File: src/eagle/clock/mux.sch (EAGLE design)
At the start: 51 parts, among them U1 SN74HC595N, U2 SN74HC595N, U3 SN74HC595N

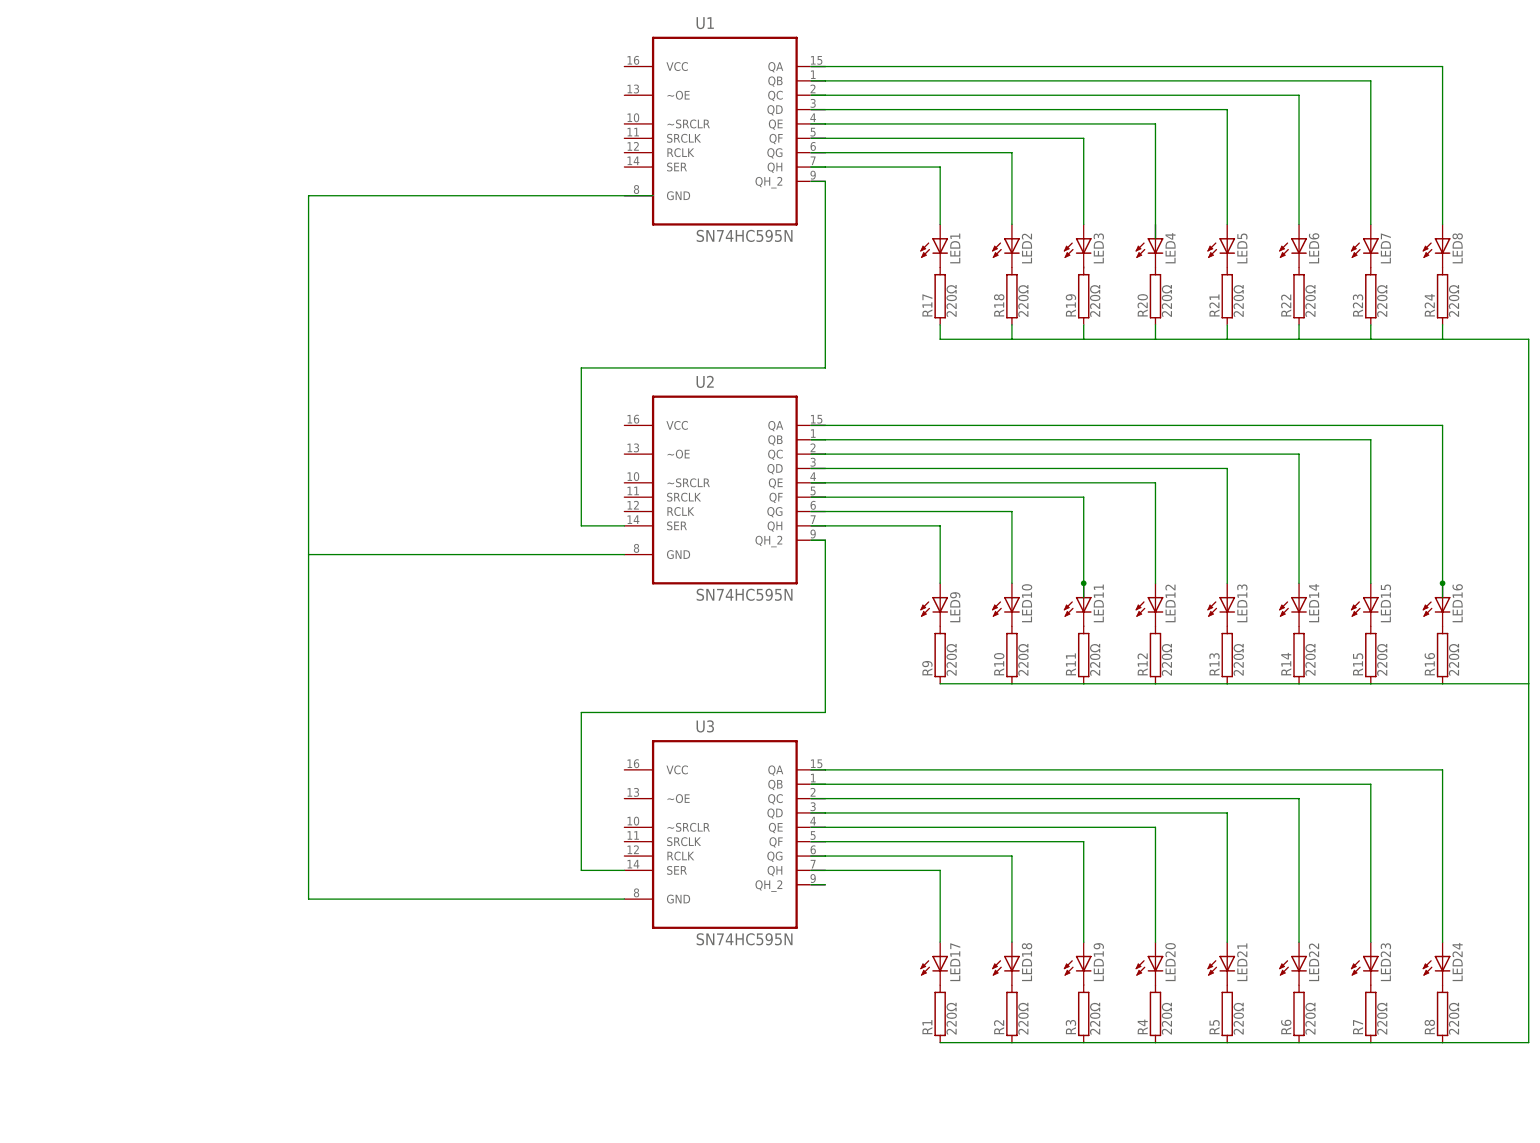
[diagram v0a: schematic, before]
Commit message: Add junctions to LEDs, SRs, and resistors
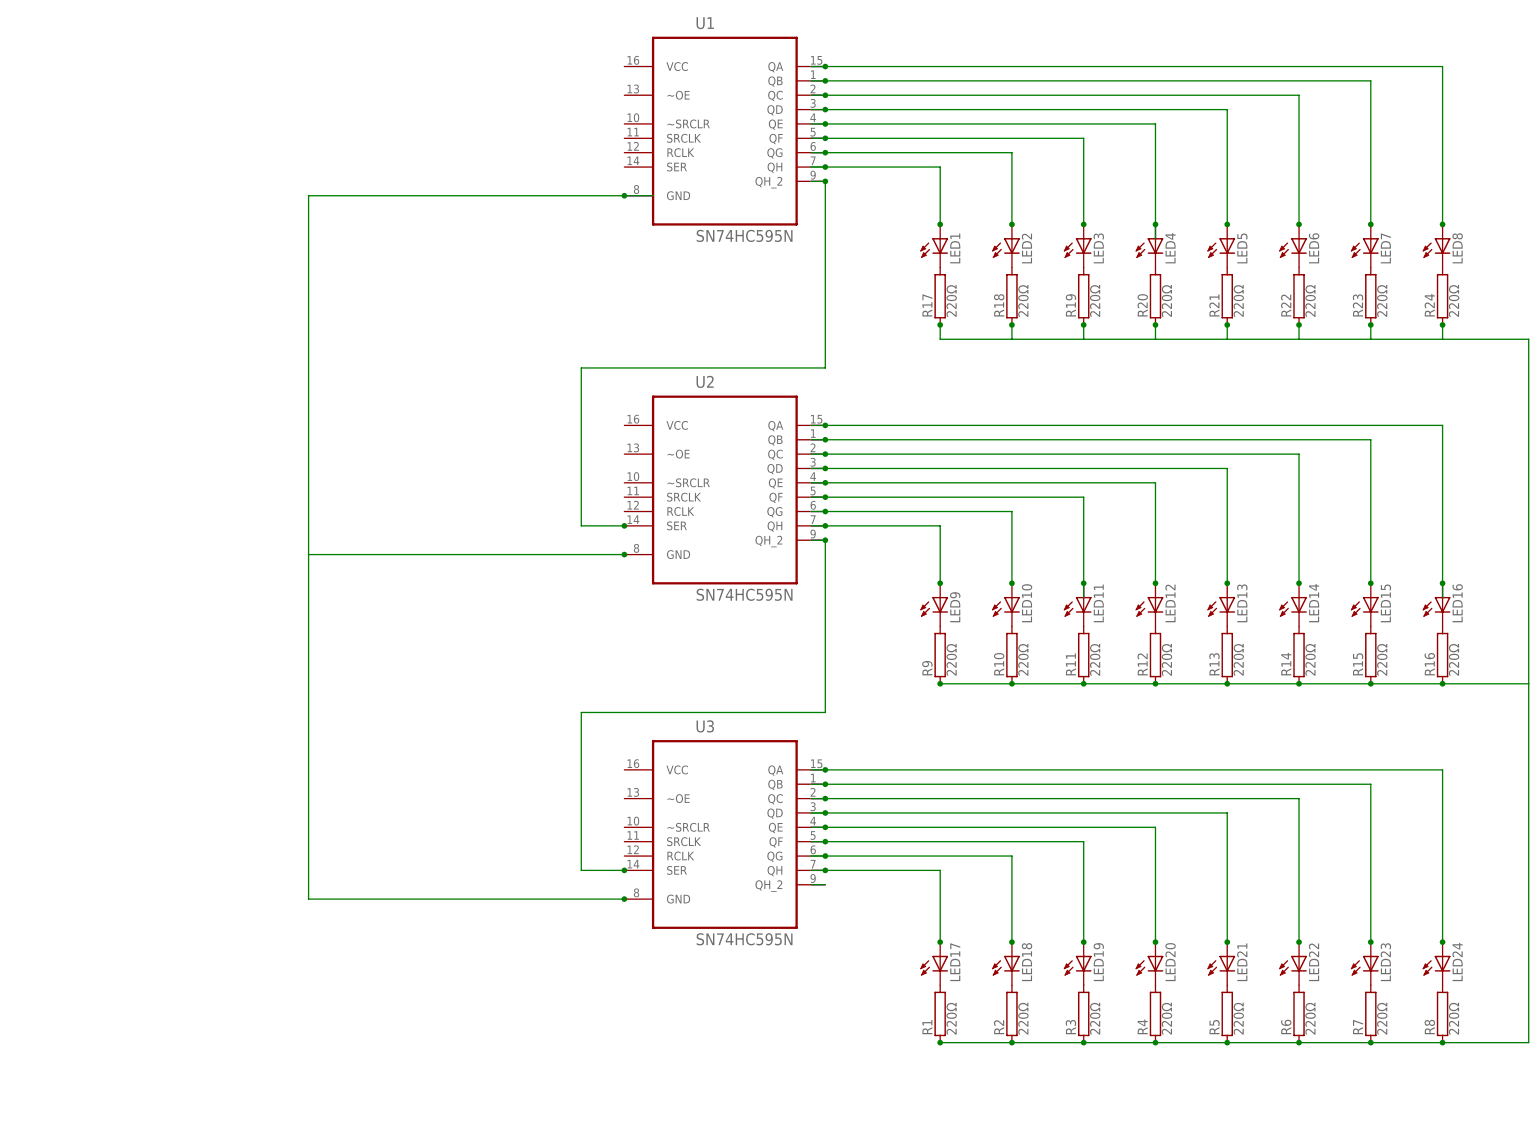
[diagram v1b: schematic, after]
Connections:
- net N$25: now also U1.QH_2
- net N$46: now also U1.GND
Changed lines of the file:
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@@
 <wire x1="152.4" y1="12.7" x2="165.1" y2="12.7" width="0.1524" layer="91"/>
 <wire x1="165.1" y1="15.24" x2="165.1" y2="12.7" width="0.1524" layer="91"/>
+<junction x="76.2" y="-48.26"/>
+<junction x="88.9" y="-48.26"/>
+<junction x="101.6" y="-48.26"/>
+<junction x="114.3" y="-48.26"/>
+<junction x="127" y="-48.26"/>
+<junction x="139.7" y="-48.26"/>
+<junction x="152.4" y="-48.26"/>
+<junction x="165.1" y="-48.26"/>
+<junction x="165.1" y="15.24"/>
+<junction x="152.4" y="15.24"/>
+<junction x="139.7" y="15.24"/>
+<junction x="127" y="15.24"/>
+<junction x="114.3" y="15.24"/>
+<junction x="101.6" y="15.24"/>
+<junction x="88.9" y="15.24"/>
+<junction x="76.2" y="15.24"/>
+<junction x="76.2" y="-111.76"/>
+<junction x="88.9" y="-111.76"/>
+<junction x="101.6" y="-111.76"/>
+<junction x="114.3" y="-111.76"/>
+<junction x="127" y="-111.76"/>
+<junction x="139.7" y="-111.76"/>
+<junction x="152.4" y="-111.76"/>
+<junction x="165.1" y="-111.76"/>
 </segment>
 </net>
@@
 <wire x1="55.88" y1="60.96" x2="165.1" y2="60.96" width="0.1524" layer="91"/>
 <wire x1="165.1" y1="60.96" x2="165.1" y2="33.02" width="0.1524" layer="91"/>
+<junction x="55.88" y="60.96"/>
+<junction x="165.1" y="33.02"/>
 </segment>
 </net>
@@
 <wire x1="55.88" y1="43.18" x2="76.2" y2="43.18" width="0.1524" layer="91"/>
 <wire x1="76.2" y1="43.18" x2="76.2" y2="33.02" width="0.1524" layer="91"/>
+<junction x="55.88" y="43.18"/>
+<junction x="76.2" y="33.02"/>
 </segment>
 </net>
@@
 <wire x1="55.88" y1="45.72" x2="88.9" y2="45.72" width="0.1524" layer="91"/>
 <wire x1="88.9" y1="45.72" x2="88.9" y2="33.02" width="0.1524" layer="91"/>
+<junction x="55.88" y="45.72"/>
+<junction x="88.9" y="33.02"/>
 </segment>
 </net>
@@
 <wire x1="55.88" y1="48.26" x2="101.6" y2="48.26" width="0.1524" layer="91"/>
 <wire x1="101.6" y1="48.26" x2="101.6" y2="33.02" width="0.1524" layer="91"/>
+<junction x="55.88" y="48.26"/>
+<junction x="101.6" y="33.02"/>
 </segment>
 </net>
@@
 <wire x1="55.88" y1="50.8" x2="114.3" y2="50.8" width="0.1524" layer="91"/>
 <wire x1="114.3" y1="50.8" x2="114.3" y2="33.02" width="0.1524" layer="91"/>
+<junction x="55.88" y="50.8"/>
+<junction x="114.3" y="33.02"/>
 </segment>
 </net>
@@
 <wire x1="55.88" y1="53.34" x2="127" y2="53.34" width="0.1524" layer="91"/>
 <wire x1="127" y1="53.34" x2="127" y2="33.02" width="0.1524" layer="91"/>
+<junction x="55.88" y="53.34"/>
+<junction x="127" y="33.02"/>
 </segment>
 </net>
@@
 <wire x1="55.88" y1="58.42" x2="152.4" y2="58.42" width="0.1524" layer="91"/>
 <wire x1="152.4" y1="58.42" x2="152.4" y2="33.02" width="0.1524" layer="91"/>
+<junction x="55.88" y="58.42"/>
+<junction x="152.4" y="33.02"/>
 </segment>
 </net>
@@
 <wire x1="55.88" y1="55.88" x2="139.7" y2="55.88" width="0.1524" layer="91"/>
 <wire x1="139.7" y1="55.88" x2="139.7" y2="33.02" width="0.1524" layer="91"/>
+<junction x="55.88" y="55.88"/>
+<junction x="139.7" y="33.02"/>
 </segment>
 </net>
@@
 <wire x1="55.88" y1="-7.62" x2="139.7" y2="-7.62" width="0.1524" layer="91"/>
 <wire x1="139.7" y1="-7.62" x2="139.7" y2="-30.48" width="0.1524" layer="91"/>
+<junction x="55.88" y="-7.62"/>
+<junction x="139.7" y="-30.48"/>
 </segment>
 </net>
@@
 <wire x1="55.88" y1="-5.08" x2="152.4" y2="-5.08" width="0.1524" layer="91"/>
 <wire x1="152.4" y1="-5.08" x2="152.4" y2="-30.48" width="0.1524" layer="91"/>
+<junction x="55.88" y="-5.08"/>
+<junction x="152.4" y="-30.48"/>
 </segment>
 </net>
@@
 <wire x1="165.1" y1="-30.48" x2="165.1" y2="-33.02" width="0.1524" layer="91"/>
 <junction x="165.1" y="-30.48"/>
+<junction x="55.88" y="-2.54"/>
 </segment>
 </net>
@@
 <wire x1="55.88" y1="-10.16" x2="127" y2="-10.16" width="0.1524" layer="91"/>
 <wire x1="127" y1="-10.16" x2="127" y2="-30.48" width="0.1524" layer="91"/>
+<junction x="55.88" y="-10.16"/>
+<junction x="127" y="-30.48"/>
 </segment>
 </net>
@@
 <wire x1="55.88" y1="-12.7" x2="114.3" y2="-12.7" width="0.1524" layer="91"/>
 <wire x1="114.3" y1="-12.7" x2="114.3" y2="-30.48" width="0.1524" layer="91"/>
+<junction x="55.88" y="-12.7"/>
+<junction x="114.3" y="-30.48"/>
 </segment>
 </net>
@@
 <wire x1="55.88" y1="-17.78" x2="88.9" y2="-17.78" width="0.1524" layer="91"/>
 <wire x1="88.9" y1="-17.78" x2="88.9" y2="-30.48" width="0.1524" layer="91"/>
+<junction x="55.88" y="-17.78"/>
+<junction x="88.9" y="-30.48"/>
 </segment>
 </net>
@@
 <wire x1="55.88" y1="-20.32" x2="76.2" y2="-20.32" width="0.1524" layer="91"/>
 <wire x1="76.2" y1="-20.32" x2="76.2" y2="-30.48" width="0.1524" layer="91"/>
+<junction x="55.88" y="-20.32"/>
+<junction x="76.2" y="-30.48"/>
 </segment>
 </net>
@@
 <wire x1="101.6" y1="-30.48" x2="101.6" y2="-33.02" width="0.1524" layer="91"/>
 <junction x="101.6" y="-30.48"/>
+<junction x="55.88" y="-15.24"/>
 </segment>
 </net>
@@
 <wire x1="55.88" y1="-78.74" x2="88.9" y2="-78.74" width="0.1524" layer="91"/>
 <wire x1="88.9" y1="-78.74" x2="88.9" y2="-93.98" width="0.1524" layer="91"/>
+<junction x="55.88" y="-78.74"/>
+<junction x="88.9" y="-93.98"/>
 </segment>
 </net>
@@
 <wire x1="55.88" y1="-76.2" x2="101.6" y2="-76.2" width="0.1524" layer="91"/>
 <wire x1="101.6" y1="-76.2" x2="101.6" y2="-93.98" width="0.1524" layer="91"/>
+<junction x="55.88" y="-76.2"/>
+<junction x="101.6" y="-93.98"/>
 </segment>
 </net>
@@
 <wire x1="55.88" y1="-71.12" x2="127" y2="-71.12" width="0.1524" layer="91"/>
 <wire x1="127" y1="-71.12" x2="127" y2="-93.98" width="0.1524" layer="91"/>
+<junction x="55.88" y="-71.12"/>
+<junction x="127" y="-93.98"/>
 </segment>
 </net>
@@
 <wire x1="55.88" y1="-68.58" x2="139.7" y2="-68.58" width="0.1524" layer="91"/>
 <wire x1="139.7" y1="-68.58" x2="139.7" y2="-93.98" width="0.1524" layer="91"/>
+<junction x="55.88" y="-68.58"/>
+<junction x="139.7" y="-93.98"/>
 </segment>
 </net>
@@
 <wire x1="55.88" y1="-66.04" x2="152.4" y2="-66.04" width="0.1524" layer="91"/>
 <wire x1="152.4" y1="-66.04" x2="152.4" y2="-93.98" width="0.1524" layer="91"/>
+<junction x="55.88" y="-66.04"/>
+<junction x="152.4" y="-93.98"/>
 </segment>
 </net>
@@
 <wire x1="55.88" y1="-63.5" x2="165.1" y2="-63.5" width="0.1524" layer="91"/>
 <wire x1="165.1" y1="-63.5" x2="165.1" y2="-93.98" width="0.1524" layer="91"/>
+<junction x="55.88" y="-63.5"/>
+<junction x="165.1" y="-93.98"/>
 </segment>
 </net>
@@
 <wire x1="55.88" y1="-73.66" x2="114.3" y2="-73.66" width="0.1524" layer="91"/>
 <wire x1="114.3" y1="-73.66" x2="114.3" y2="-93.98" width="0.1524" layer="91"/>
+<junction x="55.88" y="-73.66"/>
+<junction x="114.3" y="-93.98"/>
 </segment>
 </net>
@@
 <wire x1="55.88" y1="-81.28" x2="76.2" y2="-81.28" width="0.1524" layer="91"/>
 <wire x1="76.2" y1="-81.28" x2="76.2" y2="-93.98" width="0.1524" layer="91"/>
+<junction x="55.88" y="-81.28"/>
+<junction x="76.2" y="-93.98"/>
 </segment>
 </net>
@@
 <pinref part="U2" gate="A" pin="SER"/>
 <wire x1="12.7" y1="-20.32" x2="20.32" y2="-20.32" width="0.1524" layer="91"/>
+<pinref part="U1" gate="A" pin="QH_2"/>
+<junction x="55.88" y="40.64"/>
+<junction x="20.32" y="-20.32"/>
 </segment>
 </net>
@@
 <pinref part="U3" gate="A" pin="SER"/>
 <wire x1="12.7" y1="-81.28" x2="20.32" y2="-81.28" width="0.1524" layer="91"/>
+<junction x="55.88" y="-22.86"/>
+<junction x="20.32" y="-81.28"/>
 </segment>
 </net>
@@
 <net name="N$46" class="0">
 <segment>
-<wire x1="25.4" y1="38.1" x2="-35.56" y2="38.1" width="0.1524" layer="91"/>
+<wire x1="25.4" y1="38.1" x2="20.32" y2="38.1" width="0.1524" layer="91"/>
+<wire x1="20.32" y1="38.1" x2="-35.56" y2="38.1" width="0.1524" layer="91"/>
 <wire x1="-35.56" y1="38.1" x2="-35.56" y2="-25.4" width="0.1524" layer="91"/>
 <pinref part="U2" gate="A" pin="GND"/>
@@
 <pinref part="U3" gate="A" pin="GND"/>
 <wire x1="-35.56" y1="-86.36" x2="20.32" y2="-86.36" width="0.1524" layer="91"/>
-</segment>
-</net>
+<pinref part="U1" gate="A" pin="GND"/>
+<junction x="20.32" y="38.1"/>
+<junction x="20.32" y="-25.4"/>
+<junction x="20.32" y="-86.36"/>
+</segment>
+</net>

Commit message: Add Arduino in/out mock
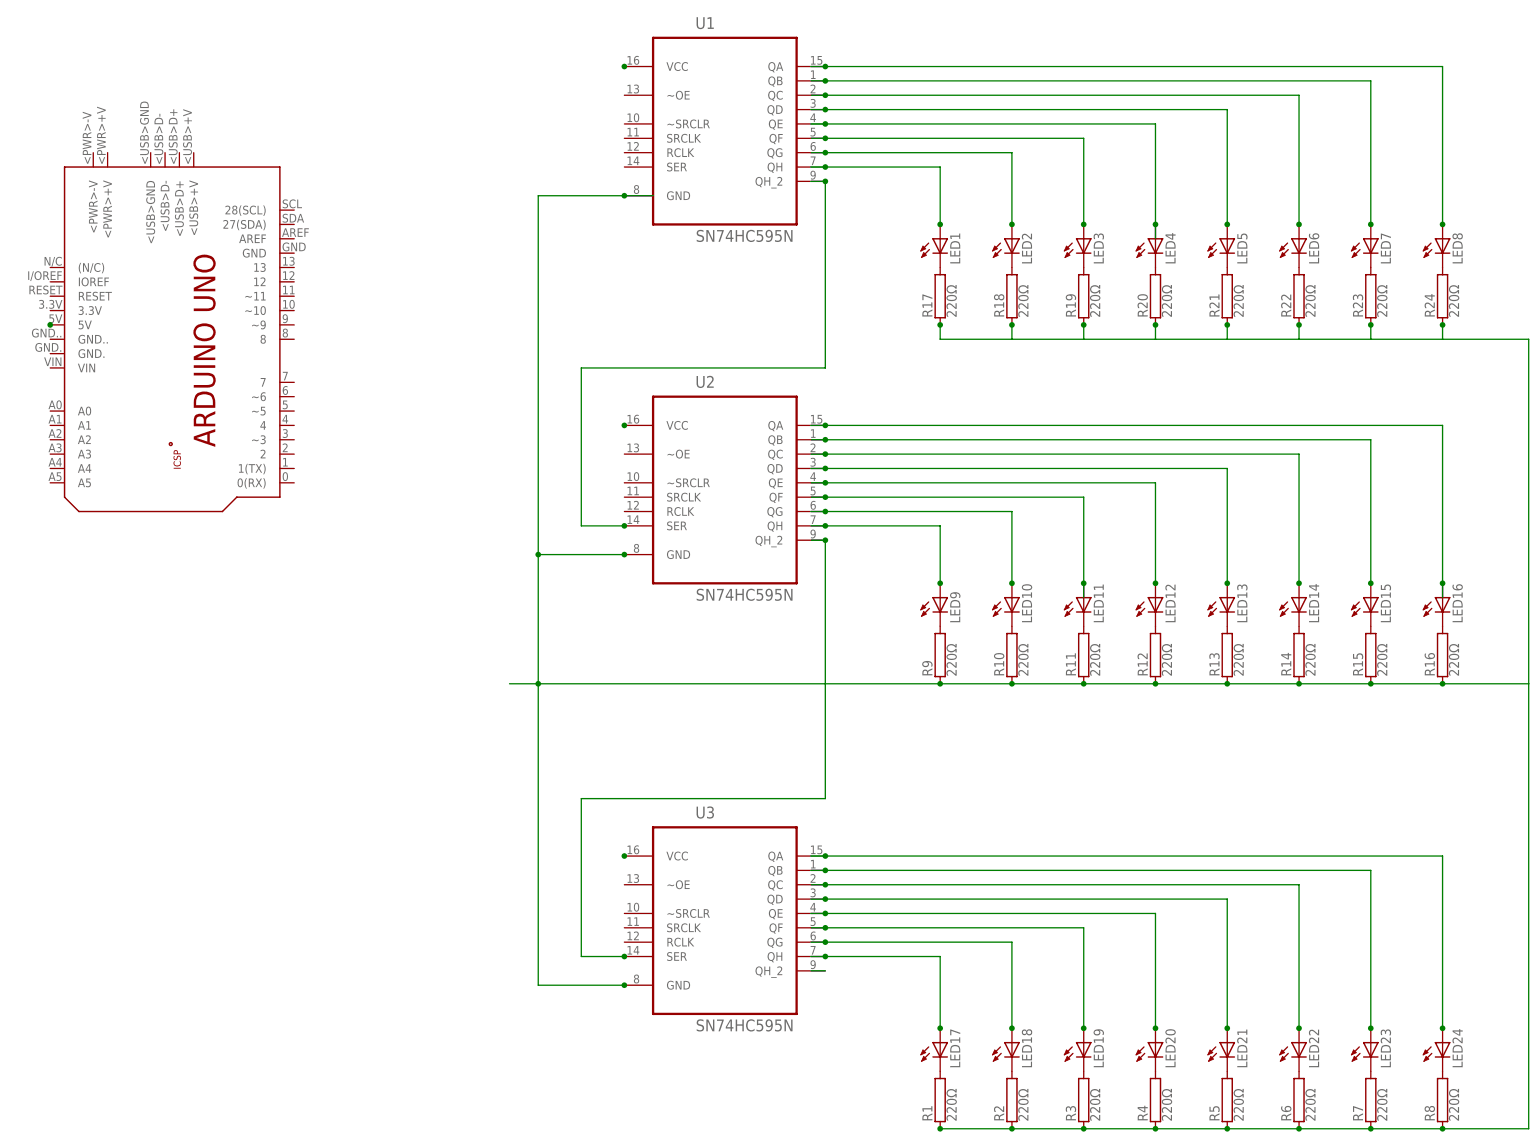
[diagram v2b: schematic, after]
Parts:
- added PCB1: ARDUINO_UNO, E14_Arduino_published:ARDUINO_UNO
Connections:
- new net N$47: U3.VCC
- new net N$48: U1.VCC
- new net N$49: PCB1.5V
- net N$26: now also U1.GND, U2.GND, U3.GND
- net N$46: now also U2.VCC; no longer U1.GND, U2.GND, U3.GND
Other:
- moved on the sheet: LED17, LED18, LED19, LED20, LED21, LED22, LED23, LED24, R1, R2, R3, R4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
